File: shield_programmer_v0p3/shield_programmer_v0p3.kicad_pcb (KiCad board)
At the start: 2 copper layers, 72.4 x 53.3 mm, 3 parts, among them P1 CONN_3X2

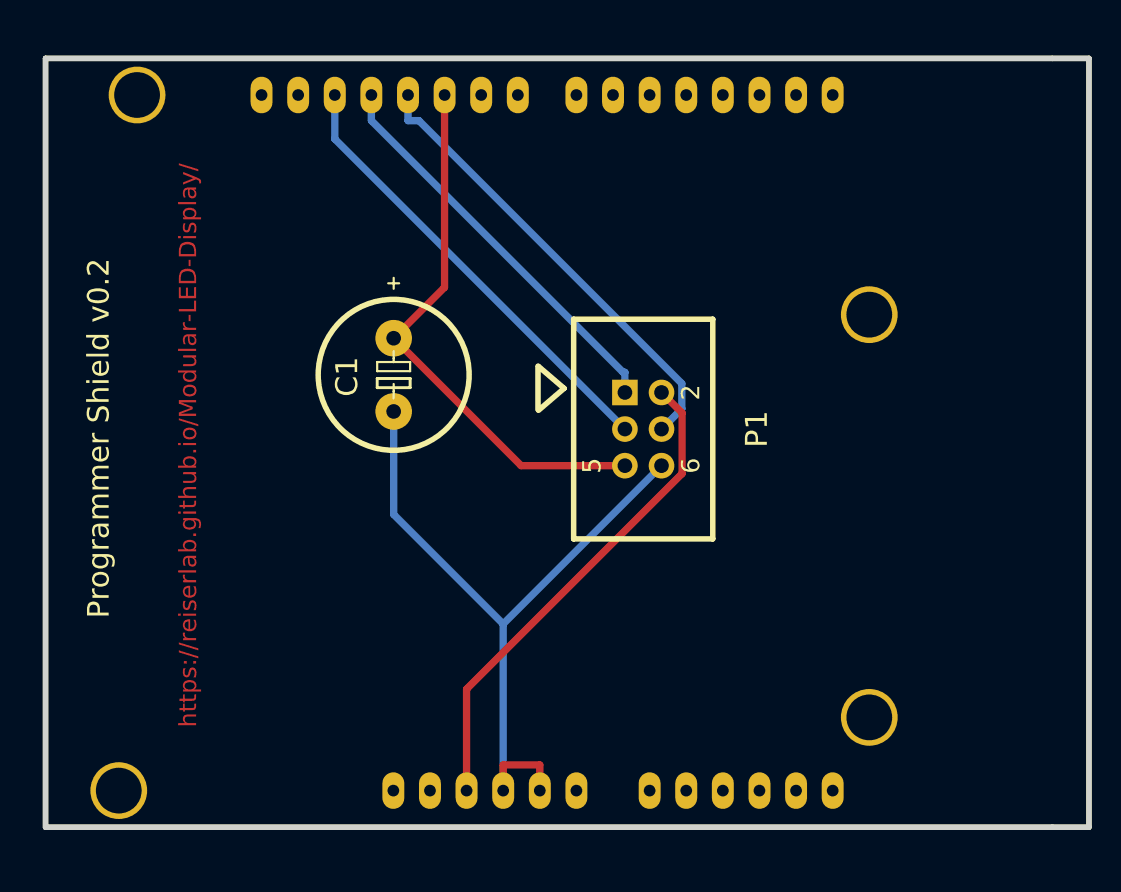
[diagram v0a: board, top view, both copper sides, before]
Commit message: new arduino shield
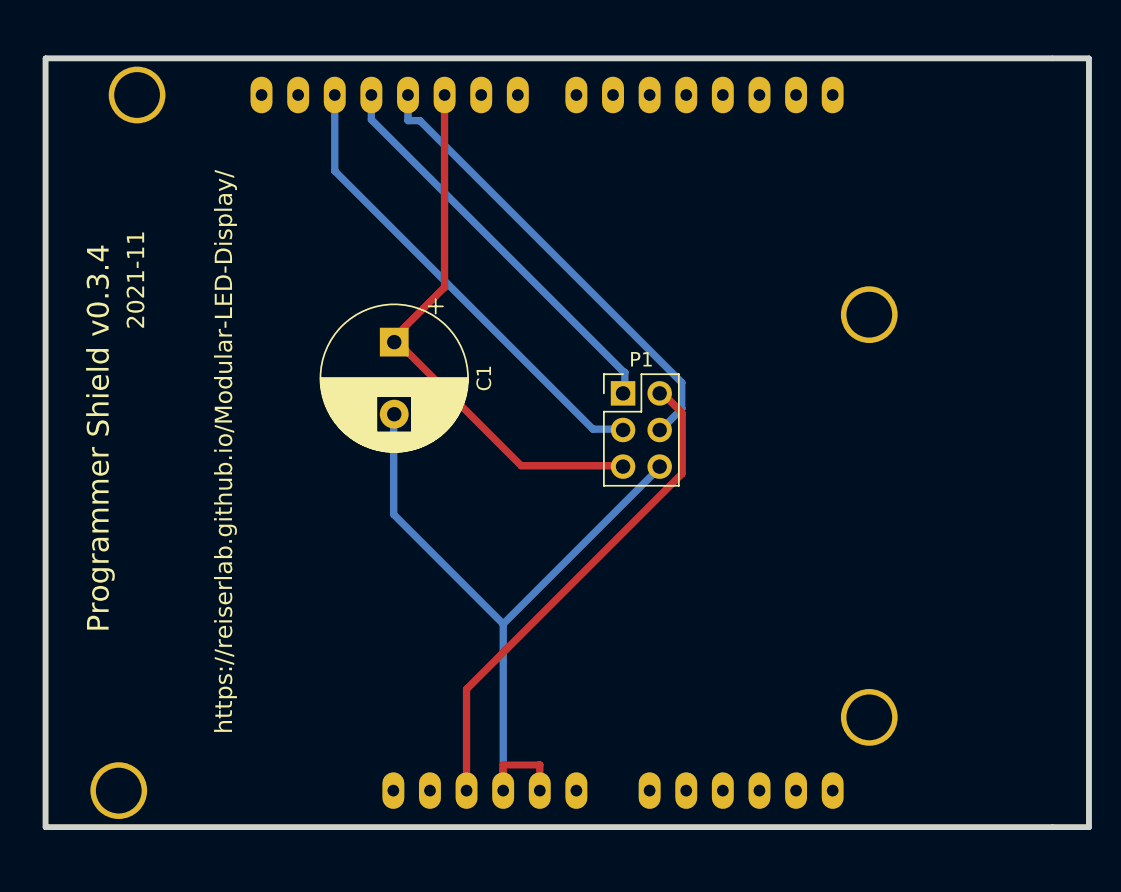
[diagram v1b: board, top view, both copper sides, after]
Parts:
- C1: footprint Capacitor_Polarized -> Capacitor_THT:CP_Radial_D10.0mm_P5.00mm
- P1: footprint 3X2_SHRD_HEADER -> Connector_PinHeader_2.54mm:PinHeader_2x03_P2.54mm_Vertical
- SHIELD1: footprint ARDUINO_SHIELD -> shield_programmer_v0p3:ARDUINO_SHIELD
- moved P1 2.84 mm to (159.8, 102.6), turned to 0 degrees
- moved C1 2.27 mm to (143.9, 99.1)
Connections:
- net /MISO renamed /CIPO
- net /MOSI renamed /COPI
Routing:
- net /SCK: track 31.5 -> 32.8 mm
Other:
- board text added: "2021-11"
- board text added: "Programmer Shield v0.3.4"
- board text removed: "Programmer Shield v0.2"

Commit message: update shield_programmer
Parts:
- C1: value CP1 -> 10uF
- SHIELD1: footprint shield_programmer_v0p3:ARDUINO_SHIELD -> Arduino:Arduino_Zero_Shield
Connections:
- C1 pad 2: /GND -> GND
- P1 pad 2: /5V -> +5V
- P1 pad 6: /GND -> GND
- SHIELD1 pad 3V3: (no net) -> unconnected-(SHIELD1-Pad3V3)
- SHIELD1 pad AREF: (no net) -> unconnected-(SHIELD1-PadAREF)
- SHIELD1 pad GND1: /GND -> GND
- SHIELD1 pad GND2: /GND -> GND
- SHIELD1 pad GND3: (no net) -> GND
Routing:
- net GND: track 0.00 -> 75.5 mm
- net /GND: track 51.1 -> 0.00 mm
- net /5V: track 34.4 -> 0.00 mm
- net +5V: track 0.00 -> 30.6 mm
- net /SCK: track 32.8 -> 27.8 mm
- net /COPI: track 32.1 -> 27.9 mm
- net /RST: track 37.9 -> 42.0 mm
- net /CIPO: track 28.0 -> 24.3 mm
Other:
- net class Default removed
- board text added: "2022-11"
- board text added: "https://reiserlab.github.io/ Modular-LED-Display/"
- board text removed: "2021-11"
- board text removed: "https://reiserlab.github.io/Modular-LED-Display/"
